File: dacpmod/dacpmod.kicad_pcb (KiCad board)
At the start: 2 copper layers, 65 x 50 mm, 69 parts, among them J1 PMOD1, J2 PMOD2, J3 POWER, J4 OUT, J5 OUT, U1 AD9744, U2 THS6024

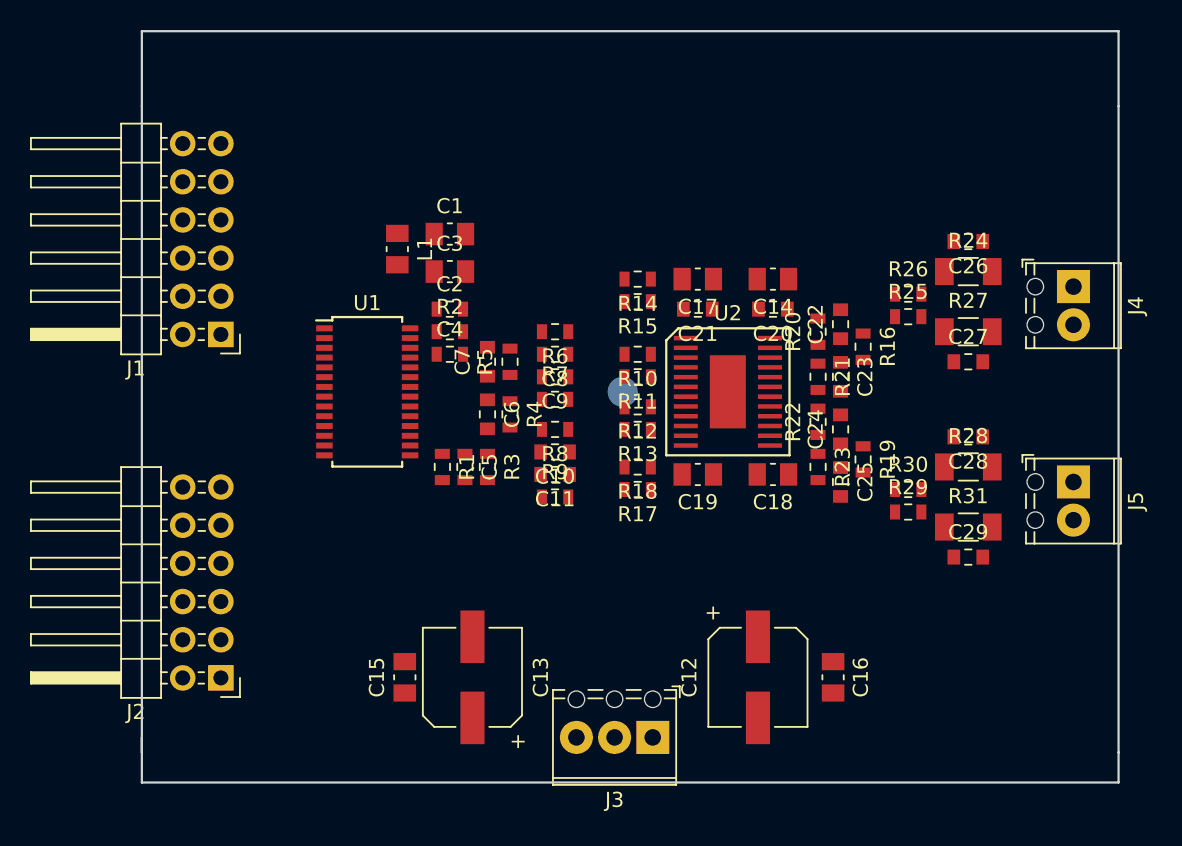
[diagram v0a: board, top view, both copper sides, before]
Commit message: DAC+VDSL PMOD routed
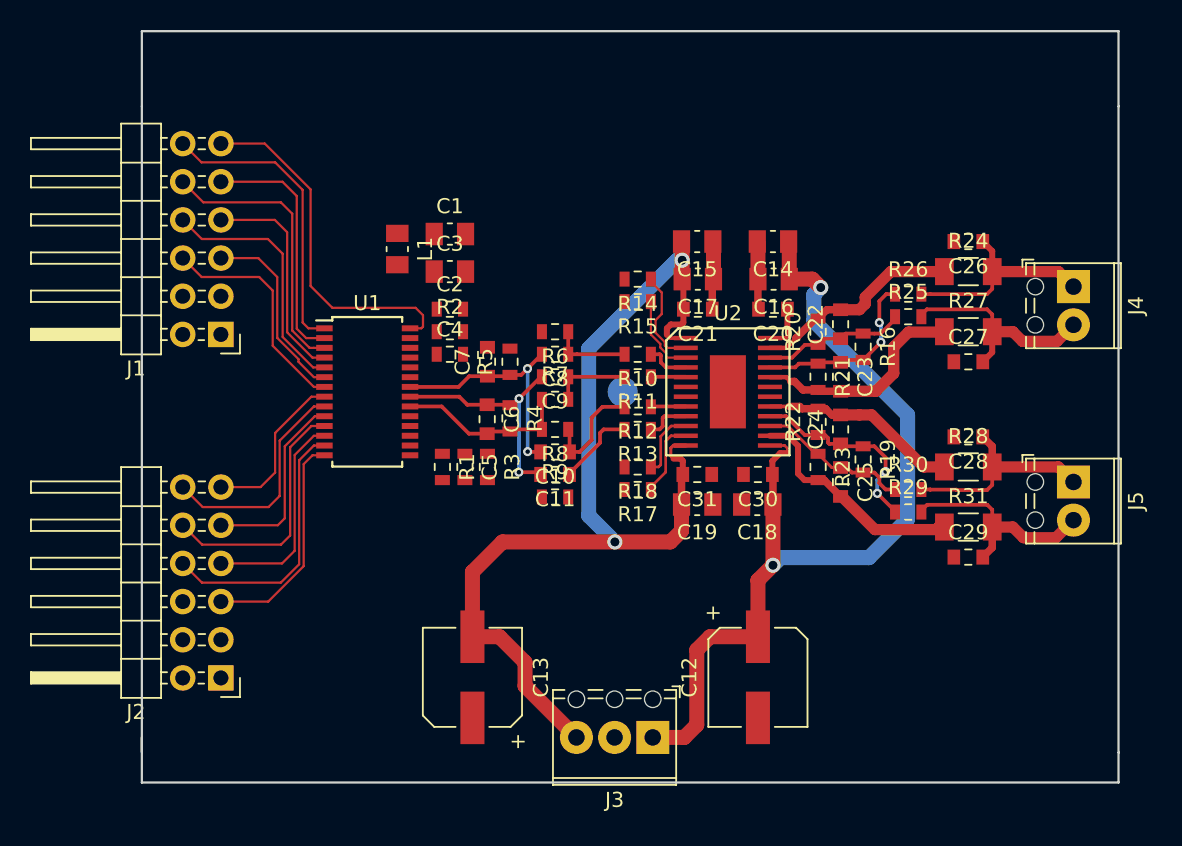
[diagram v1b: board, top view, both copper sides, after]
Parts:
- added C30: 10n, Capacitor_SMD:C_0603_1608Metric_Pad0.84x1.00mm_HandSolder, F.Cu at (84.0, 52.5)
- added C31: 10n, Capacitor_SMD:C_0603_1608Metric_Pad0.84x1.00mm_HandSolder, F.Cu at (80.0, 52.5)
- moved C15 34.9 mm to (80.0, 37.0), turned to 180 degrees
- moved C16 26.8 mm to (85.0, 39.5), turned to 180 degrees
- moved C14 2.50 mm to (85.0, 37.0)
- moved C18 2.26 mm to (84.0, 54.5)
- moved C19 2.00 mm to (80.0, 54.5)
- moved C6 0.32 mm to (66.0, 48.8)
- moved R4 0.27 mm to (67.5, 48.8)
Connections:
- J1 pad 1: /D0 -> /CLK
- J1 pad 2: /D2 -> /D12
- J1 pad 3: /D4 -> /D10
- J1 pad 4: /D6 -> /D8
- J1 pad 7: /D1 -> /D13
- J1 pad 8: /D3 -> /D11
- J1 pad 9: /D5 -> /D9
- J2 pad 1: /D8 -> /D6
- J2 pad 2: /D10 -> /D4
- J2 pad 3: /D12 -> /D2
- J2 pad 4: /CLK -> /D0
- J2 pad 7: /D9 -> /D5
- J2 pad 8: /D11 -> /D3
- J2 pad 9: /D13 -> /D1
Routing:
- net VEE: track 0.00 -> 68.7 mm, vias 0 -> 2
- net VCC: track 0.00 -> 63.9 mm, vias 0 -> 2
- net /CLK: track 0.00 -> 23.6 mm
- net GND: track 0.00 -> 20.7 mm
- net /D13: track 0.00 -> 19.7 mm
- net /D11: track 0.00 -> 18.6 mm
- net /D1: track 0.00 -> 17.8 mm
- net /D9: track 0.00 -> 16.7 mm
- net /D3: track 0.00 -> 16.7 mm
- net /D12: track 0.00 -> 16.4 mm
- net Net-(C11-Pad2): track 0.00 -> 16.2 mm, vias 0 -> 2
- net Net-(C10-Pad2): track 0.00 -> 16.1 mm, vias 0 -> 2
- net Net-(C25-Pad2): track 0.00 -> 15.3 mm
- net /D7: track 0.00 -> 15.1 mm
- net /D5: track 0.00 -> 14.9 mm
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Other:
- net class Default: clearance 0.2 -> 0.15; trace_width 0.25 -> 0.15; via_dia 0.8 -> 0.6; via_drill 0.4 -> 0.3
- rule trace_clearance: 0.2 -> 0.15
- rule trace_min: 0.2 -> 0.15
- rule via_min_size: 0.4 -> 0.6
